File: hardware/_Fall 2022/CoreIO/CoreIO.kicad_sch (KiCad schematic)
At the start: 20 parts

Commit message: add IO board development
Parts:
- removed D?: LED, symbol Device:LED
- removed H? (x2): MountingHole_Pad, symbol Mechanical:MountingHole_Pad
- removed Q?: Q_NJFET_DGS, symbol Device:Q_NJFET_DGS
- removed R? (x6): R, symbol Device:R
- removed U?: XT30UPB-M, XT30UPB-M, symbol XT30:XT30UPB-M
- added H3, H4: Pad, symbol Mechanical:MountingHole_Pad
- added J1: Conn_01x09_Female, Connector_JST:JST_PH_S9B-PH-K_1x09_P2.00mm_Horizontal, symbol Connector:Conn_01x09_Female
- added Q?: Q_NJFET_DGS, symbol Device:Q_NJFET_DGS
- added R2, R3, R? (x3): R, symbol Device:R
- added U?: XT30UPB-M, XT30UPB-M, symbol XT30:XT30UPB-M
- H1, H2: renamed from H?; value MountingHole_Pad -> Pad
- gave numbers to parts that had none: 7
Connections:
- net +3.3V: now also H1.1; no longer D1.2 (A), D2.2 (A), Q1.1 (D)
- net GND: now also D2.1 (K), Q1.2 (G), R1.1, R8.2, J1.9 (Pin_9), Q?.3 (S), R?.1, R?.2; no longer H2.1
- net Teensy Out renamed CONT 1
- net CONT 1: now also J1.3 (Pin_3), R?.2; no longer Q1.2 (G)
- new net: H4.1, R2.2, R3.2
- new net: Q?.1 (D), R?.1, U?.P$1 (+)
- new net ARM: J1.1 (Pin_1), R2.1
- new net BAT1 V: J1.7 (Pin_7)
- new net BAT2 V: J1.6 (Pin_6)
- new net CONT 2: J1.2 (Pin_2)
- new net PYRO 1: J1.5 (Pin_5), Q?.2 (G), R?.1, R?.2
- new net PYRO 2: J1.4 (Pin_4)
- new net REG. 3.3: D1.2 (A), H2.1, J1.8 (Pin_8)
- new net VCC: H3.1
- new net V_IGNITOR: D2.2 (A), Q1.1 (D), R3.1, U?.P$2 (-)
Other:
- note added: "ARMING SWITCH"
- note added: "Arming Safe Switch"
- note added: "Master Power Switch"
- note added: "POWER SWITCH"
- note added: "TO CORE1"
- moved on the sheet: D1, D2, H1, H2, Q1, R1, R6, R8, U1

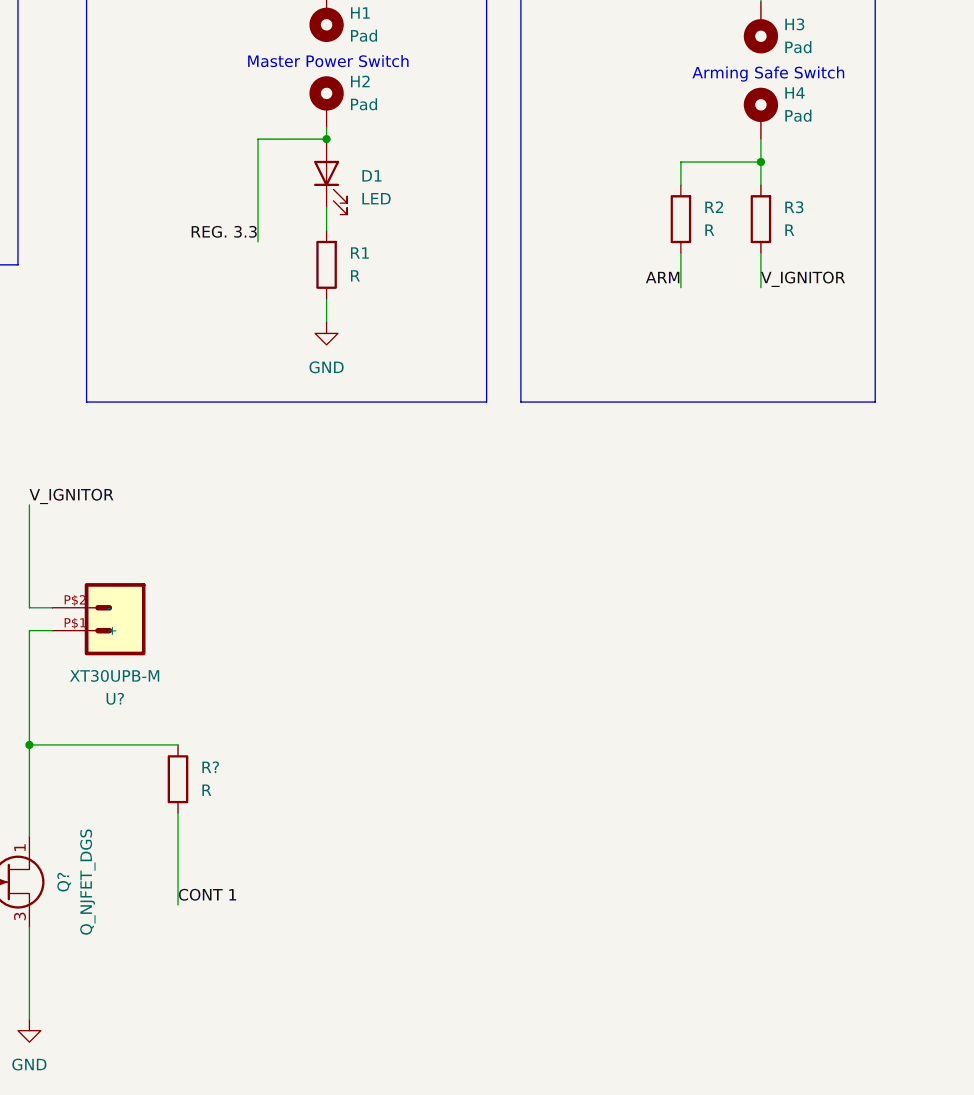
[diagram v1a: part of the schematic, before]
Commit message: add pull down resistors to IO board
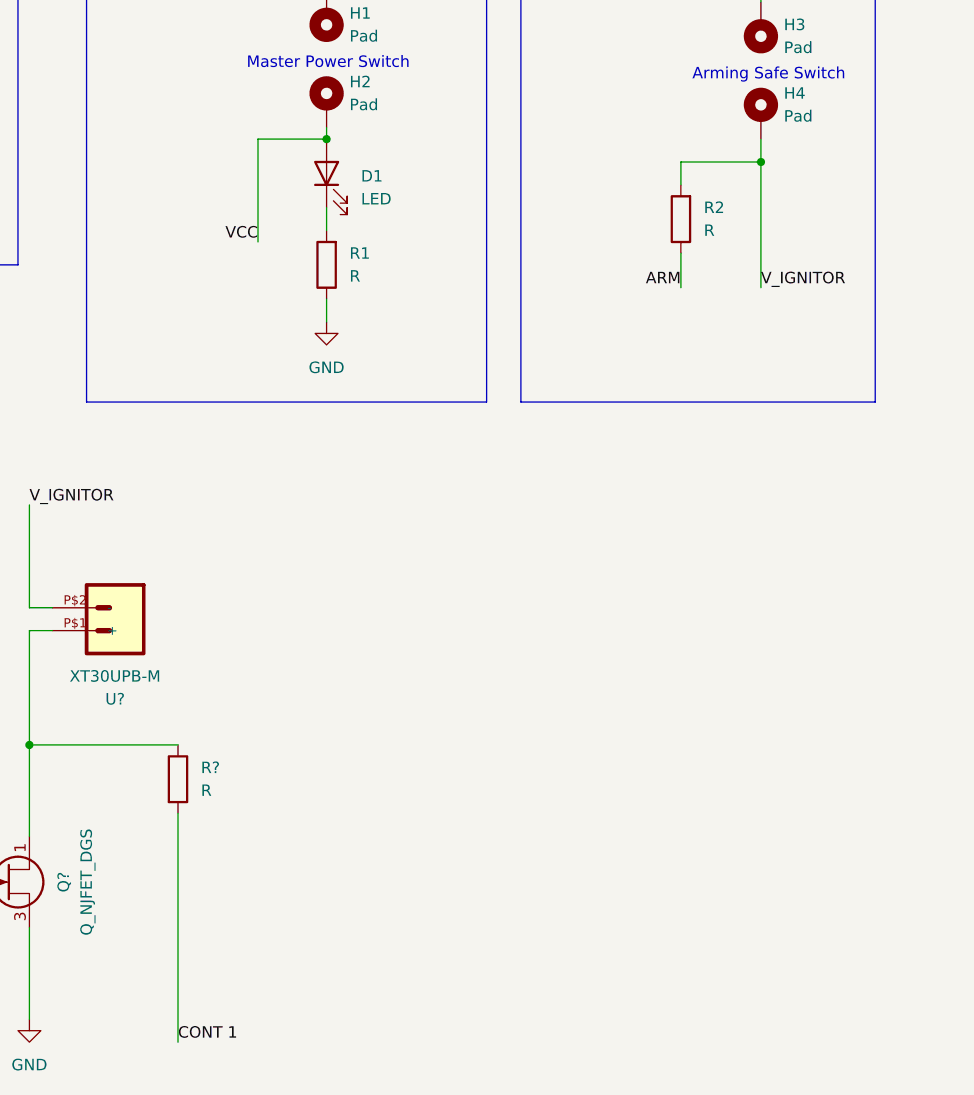
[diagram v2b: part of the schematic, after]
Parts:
- removed R3: R, symbol Device:R
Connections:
- net REG. 3.3: no longer D1.2 (A), H2.1
- net VCC: now also D1.2 (A), H2.1
- net V_IGNITOR: now also H4.1, R2.2
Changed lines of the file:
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@@
-    (stroke (width 0) (type default) (color 0 0 0 0))
-  )
-  (wire (pts (xy 78.74 130.81) (xy 78.74 140.97))
     (stroke (width 0) (type default) (color 0 0 0 0))
   )
@@
     (stroke (width 0) (type default) (color 0 0 0 0))
   )
+  (wire (pts (xy 78.74 130.81) (xy 78.74 156.21))
+    (stroke (width 0) (type default) (color 0 0 0 0))
+  )
   (wire (pts (xy 39.37 46.99) (xy 43.18 46.99))
     (stroke (width 0) (type default) (color 0 0 0 0))
   )
-  (wire (pts (xy 143.51 68.58) (xy 143.51 72.39))
-    (stroke (width 0) (type default) (color 0 0 0 0))
-  )
   (wire (pts (xy 49.53 149.86) (xy 49.53 153.67))
     (stroke (width 0) (type default) (color 0 0 0 0))
@@
     (stroke (width 0) (type default) (color 0 0 0 0))
   )
-  (wire (pts (xy 143.51 58.42) (xy 143.51 60.96))
+  (wire (pts (xy 143.51 58.42) (xy 143.51 72.39))
     (stroke (width 0) (type default) (color 0 0 0 0))
   )
@@
     (effects (font (size 1.27 1.27)) (justify left bottom))
   )
-  (label "CONT 1" (at 78.74 140.97 0)
+  (label "CONT 1" (at 78.74 156.21 0)
     (effects (font (size 1.27 1.27)) (justify left bottom))
   )
@@
     (effects (font (size 1.27 1.27)) (justify left bottom))
   )
-  (label "REG. 3.3" (at 87.63 67.31 180)
+  (label "VCC" (at 87.63 67.31 180)
     (effects (font (size 1.27 1.27)) (justify right bottom))
   )
@@
     (pin "2")
   )
-  (symbol (lib_id "Device:R") (at 143.51 64.77 180) (unit 1)
-    (in_bom yes) (on_board yes) (fields_autoplaced)
-    (property "Reference" "R3" (id 0) (at 146.05 63.4999 0)
-      (effects (font (size 1.27 1.27)) (justify right))
-    )
-    (property "Value" "R" (id 1) (at 146.05 66.0399 0)
-      (effects (font (size 1.27 1.27)) (justify right))
-    )
-    (property "Footprint" "" (id 2) (at 145.288 64.77 90)
-      (effects (font (size 1.27 1.27)) hide)
-    )
-    (property "Datasheet" "~" (id 3) (at 143.51 64.77 0)
-      (effects (font (size 1.27 1.27)) hide)
-    )
-    (pin "1")
-    (pin "2")
-  )
   (sheet_instances
     (path "/" (page "1"))
@@
       (reference "R2") (unit 1) (value "R") (footprint "")
     )
-    (path "/f80bd027-8256-40a7-b45f-3651fe2091ad"
-      (reference "R3") (unit 1) (value "R") (footprint "")
-    )
     (path "/c08d33b1-a9c8-4604-b7b9-2d6540826e69"
